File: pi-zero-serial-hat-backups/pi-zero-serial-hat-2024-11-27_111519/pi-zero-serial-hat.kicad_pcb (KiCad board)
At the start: 2 copper layers, 65 x 55.5 mm, 56 parts, among them J1 Conn_02x20_Counter_Clockwise, J2 Screw_Terminal_01x03, J3 Conn_01x02_Pin, J4 Conn_01x02_Pin, J5 Screw_Terminal_01x02, Q1 AOD4184, Q2 AOD4184, U1 MAX13487EESAT, U2 CX8571

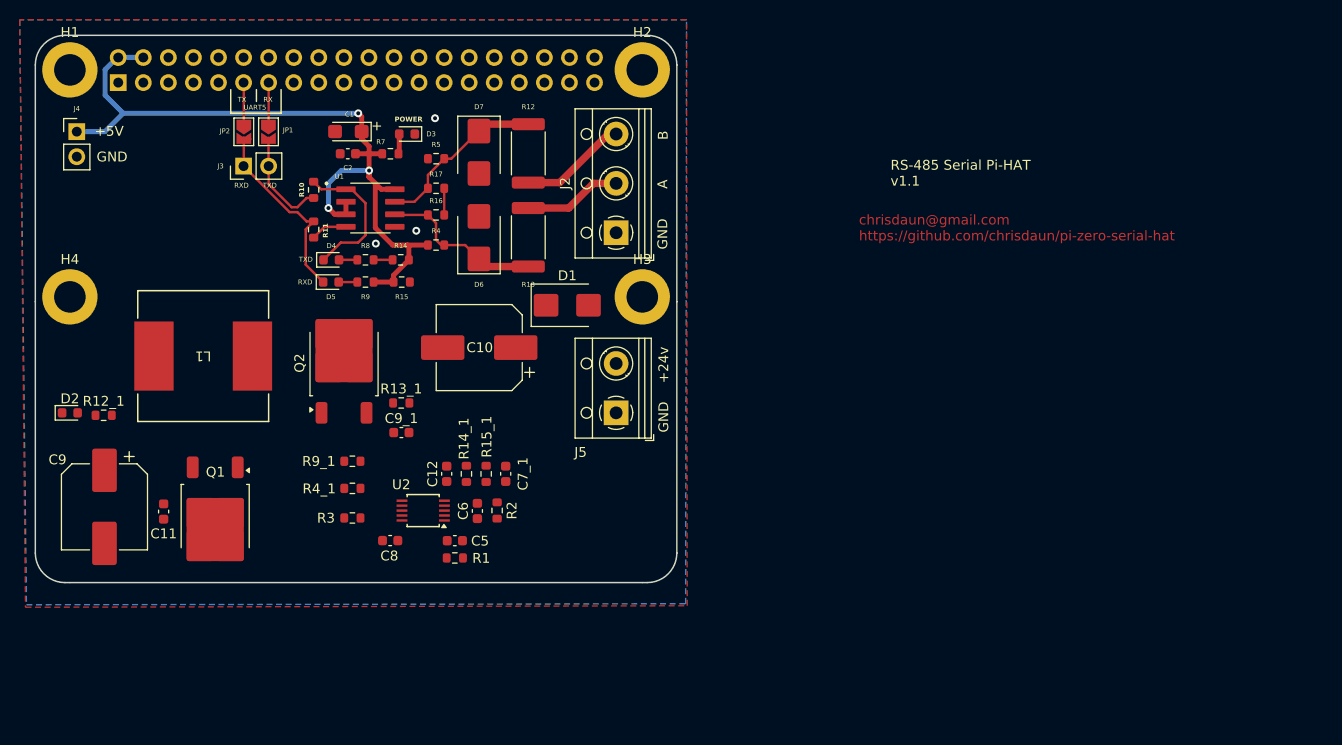
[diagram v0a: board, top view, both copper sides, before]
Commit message: Added schematic from reversed board
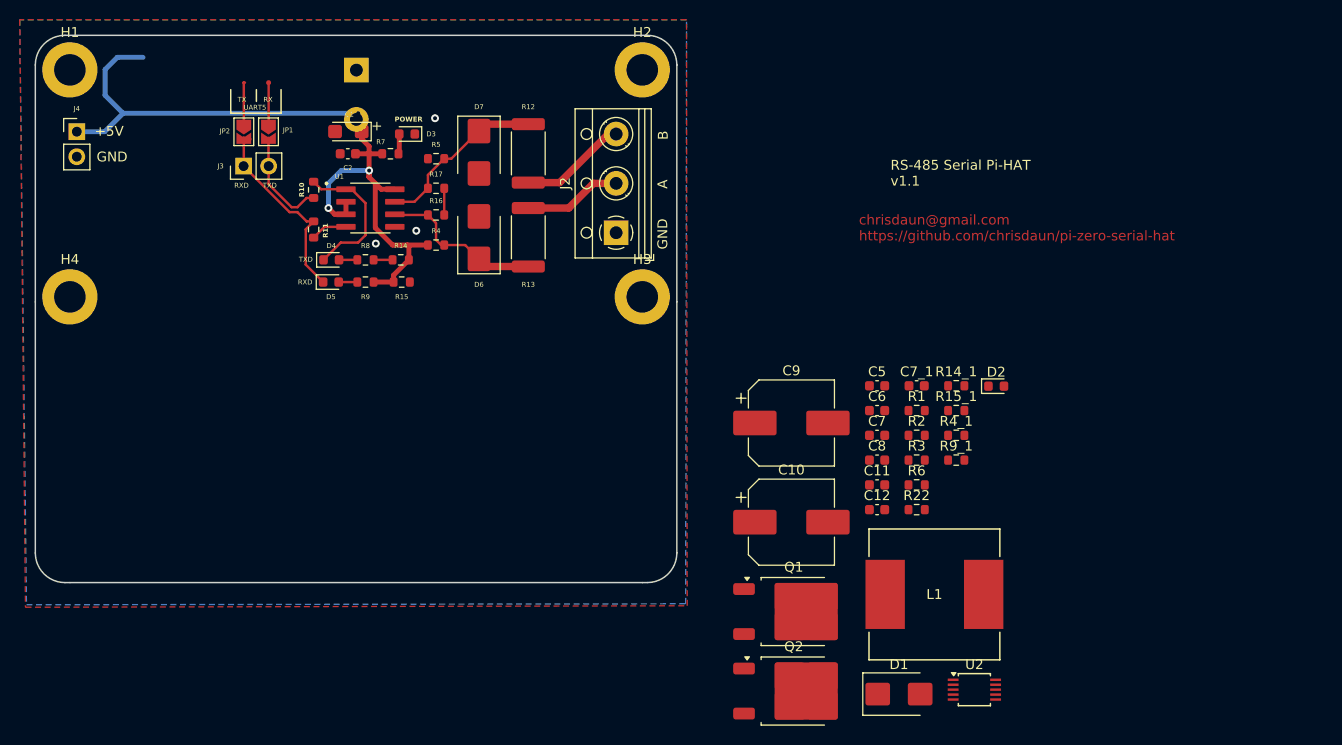
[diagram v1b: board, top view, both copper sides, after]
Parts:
- removed C9_1: C, Capacitor_SMD:C_0603_1608Metric
- removed J5: Screw_Terminal_01x02, TerminalBlock_RND:TerminalBlock_RND_205-00012_1x02_P5.00mm_Horizontal
- removed R12_1: 018, Resistor_SMD:R_0603_1608Metric
- removed R13_1: 4R7, Resistor_SMD:R_0603_1608Metric
- added C7: C, Capacitor_SMD:C_0603_1608Metric, F.Cu at (202.8, 131.6)
- added R22: R, Resistor_SMD:R_0603_1608Metric, F.Cu at (206.8, 139.1)
- added R6: R, Resistor_SMD:R_0603_1608Metric, F.Cu at (206.8, 136.6)
- C10: value 100uF 50v -> C_Polarized
- C9: value 470uF 16v -> C_Polarized
- J1: value Conn_02x20_Counter_Clockwise -> Screw_Terminal_01x02; footprint lib:PinSocket_2x20_P2.54mm_Vertical_Centered_Anchor -> TerminalBlock_RND:TerminalBlock_RND_205-00012_1x02_P5.00mm_Horizontal
- moved D2 93.9 mm to (214.9, 126.6)
- moved L1 77.9 mm to (208.6, 147.7), turned to 0 degrees
- moved C11 72.3 mm to (202.8, 136.6), turned to 0 degrees
- moved C9 70.1 mm to (194.1, 130.3), turned to 0 degrees
- moved R4_1 61.4 mm to (210.8, 131.6)
- moved R9_1 61.2 mm to (210.8, 134.1)
- moved Q1 59.4 mm to (194.4, 149.5), turned to 0 degrees
- moved U2 58.7 mm to (212.7, 157.4), turned to 0 degrees
- moved R3 57.5 mm to (206.8, 134.1)
- moved Q2 56.4 mm to (194.4, 157.5), turned to 0 degrees
- moved D1 51.8 mm to (205.0, 157.8)
- moved R14_1 50.4 mm to (210.8, 126.6), turned to 0 degrees
- moved C8 50.0 mm to (202.8, 134.1)
- moved R1 49.1 mm to (206.8, 129.1)
- moved R15_1 48.1 mm to (210.8, 129.1), turned to 0 degrees
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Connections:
- J1 pad 1: unconnected-(J1-Pin_1-Pad1) -> GND
- J1 pad 2: unconnected-(J1-Pin_2-Pad2) -> +24V
- L1 pad 1: Net-(Q1-S) -> Net-(Q1-D)
- Q1 pad 2: Net-(D1-K) -> Net-(Q1-D)
- Q1 pad 3: Net-(Q1-S) -> GND
- Q2 pad 2: Net-(Q1-S) -> Net-(D1-K)
- Q2 pad 3: GND -> Net-(Q1-D)
- R3 pad 2: Net-(Q1-S) -> Net-(Q1-D)
- R4_1 pad 2: Net-(Q1-G) -> Net-(Q2-G)
- R9_1 pad 2: Net-(Q2-G) -> Net-(Q1-G)
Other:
- board text removed: "+24v"
